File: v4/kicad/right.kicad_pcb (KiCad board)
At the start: 2 copper layers, 158 x 119 mm, 72 parts

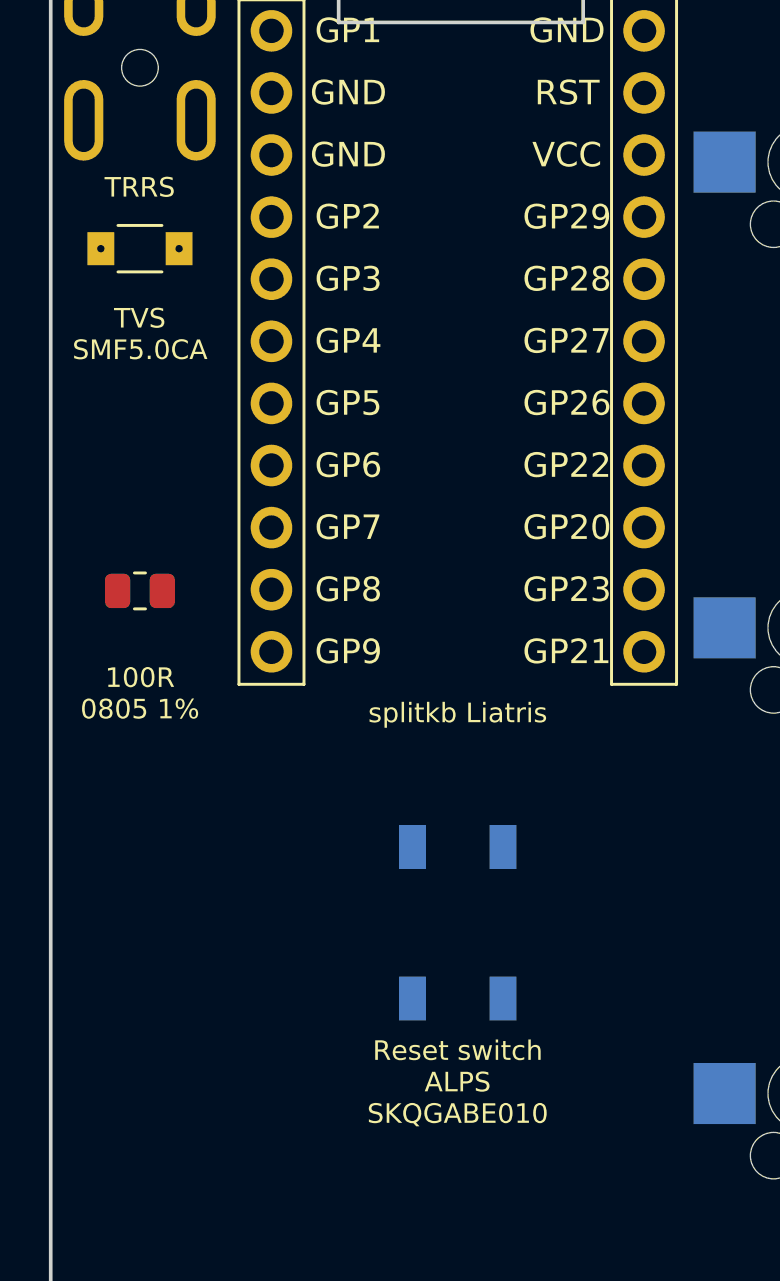
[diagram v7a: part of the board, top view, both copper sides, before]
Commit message: v4: add component silkscreen labels
Single-sided labels placed on each part's mount side: MCU and TRRS on
the front, all SMD parts (diodes, resistor, TVS, reset switch) on the
back (mirrored so they read from the back). Adds reset GND/RST pad
labels and a diode + hotswap-socket part-number label in each half's
bottom-pinky margin.
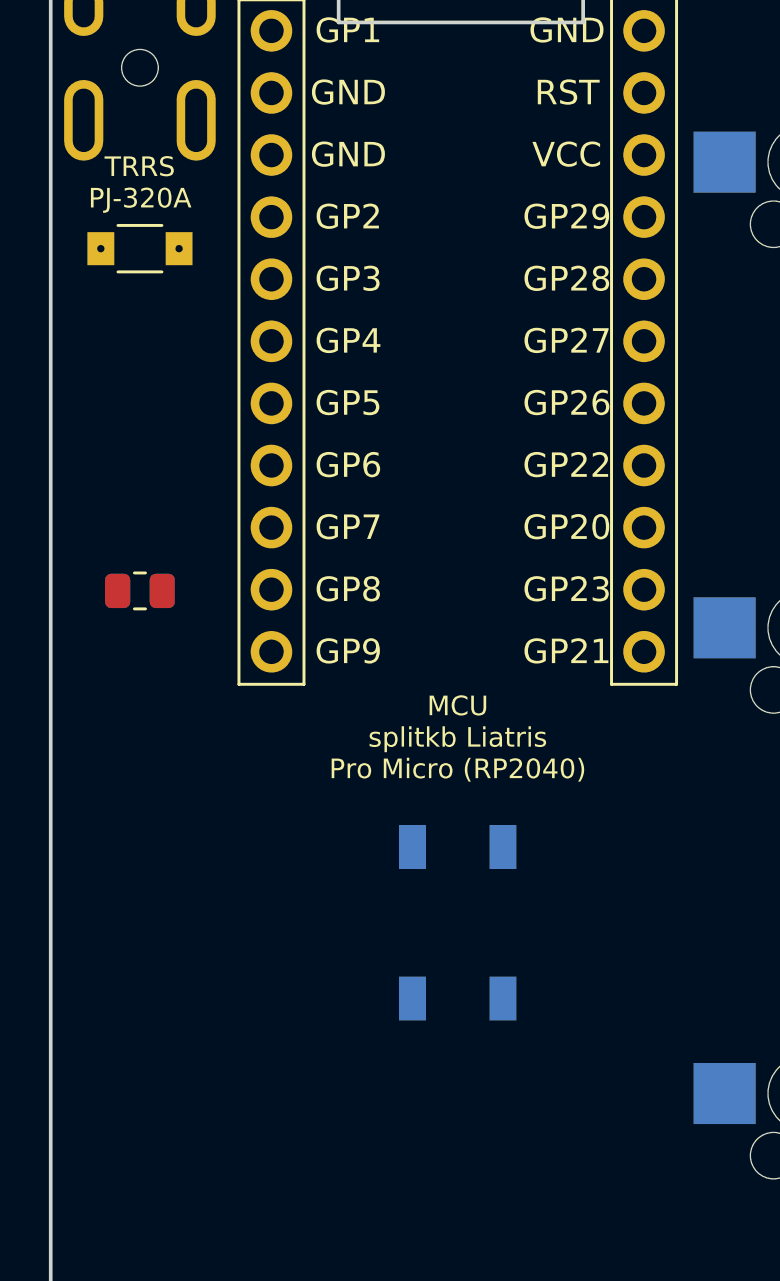
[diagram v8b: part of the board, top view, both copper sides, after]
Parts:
- D33: value SMF3.3CA -> SMF5.0CA
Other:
- board text added: "GND"
- board text added: "MCU splitkb Liatris Pro Micro (RP2040)"
- board text added: "RST"
- board text added: "Reset switch ALPS SKQGABE010 5.2mm"
- board text added: "Resistor 100R 1% UNI-ROYAL 0805W8F- 1000T5E 0805"
- board text added: "Socket Kailh CPG151101S11 MX hotswap Diode 1N4148W SOD-123"
- board text added: "TRRS PJ-320A"
- board text added: "TVS Littelfuse SMF5.0CA SOD-123FL"
- board text removed: "100R 0805 1%"
- board text removed: "Reset switch ALPS SKQGABE010"
- board text removed: "TRRS"
- board text removed: "TVS SMF5.0CA"
- board text removed: "splitkb Liatris"
